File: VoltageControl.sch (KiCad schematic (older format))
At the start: 7 parts, among them U201 LMV358

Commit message: updated schematic capacitor symbols to use new default library symbols
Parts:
- C201: Fieldname (none) -> Value
- R201, R202, R203: symbol R -> R-RESCUE-CurrentSinkOrSwim
- RV201: symbol POT -> POT-RESCUE-CurrentSinkOrSwim
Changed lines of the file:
@@
 EESchema Schematic File Version 2
+LIBS:CurrentSinkOrSwim-rescue
 LIBS:power
 LIBS:device
@@
 LIBS:memory
 LIBS:xilinx
-LIBS:special
 LIBS:microcontrollers
 LIBS:dsp
@@
 $EndComp
 $Comp
-L R R201
+L R-RESCUE-CurrentSinkOrSwim R201
 U 1 1 54DB1D0A
 P 4100 2650
@@
 	3800 5550 9850 5550
 $Comp
-L POT RV201
+L POT-RESCUE-CurrentSinkOrSwim RV201
 U 1 1 54DB1D22
 P 3800 3550
@@
 	1    0    0    -1
 $EndComp
-$Comp
-L C C201
-U 1 1 54DB1D32
-P 5150 2400
-F 0 "C201" H 5200 2500 50  0000 L CNN
-F 1 ".1" H 5200 2300 50  0000 L CNN
-F 2 "SMD_Packages:SMD-0805" H 5188 2250 30  0001 C CNN
-F 3 "" H 5150 2400 60  0000 C CNN
-	1    5150 2400
-	1    0    0    -1
-$EndComp
 Wire Wire Line
 	5150 1950 5150 2200
 Connection ~ 5150 1950
-Wire Wire Line
-	5150 2650 5150 2600
 Text GLabel 2650 1350 0    60   Input ~ 0
 2.7V
@@
 $EndComp
 $Comp
-L R R202
+L R-RESCUE-CurrentSinkOrSwim R202
 U 1 1 54DB1EC2
 P 8700 3450
@@
 $EndComp
 $Comp
-L R R203
+L R-RESCUE-CurrentSinkOrSwim R203
 U 1 1 54DB1F3A
 P 8700 4300
@@
 	4100 2900 4100 3550
 Connection ~ 4100 3550
+$Comp
+L C C201
+U 1 1 57B0D6FD
+P 5150 2350
+F 0 "C201" H 5175 2450 50  0000 L CNN
+F 1 ".1" H 5175 2250 50  0000 L CNN
+F 2 "SMD_Packages:SMD-0805" H 5188 2200 50  0001 C CNN
+F 3 "" H 5150 2350 50  0000 C CNN
+F 4 "Value" H 5150 2350 60  0001 C CNN "Fieldname"
+	1    5150 2350
+	1    0    0    -1
+$EndComp
+Wire Wire Line
+	5150 2500 5150 2650
 $EndSCHEMATC

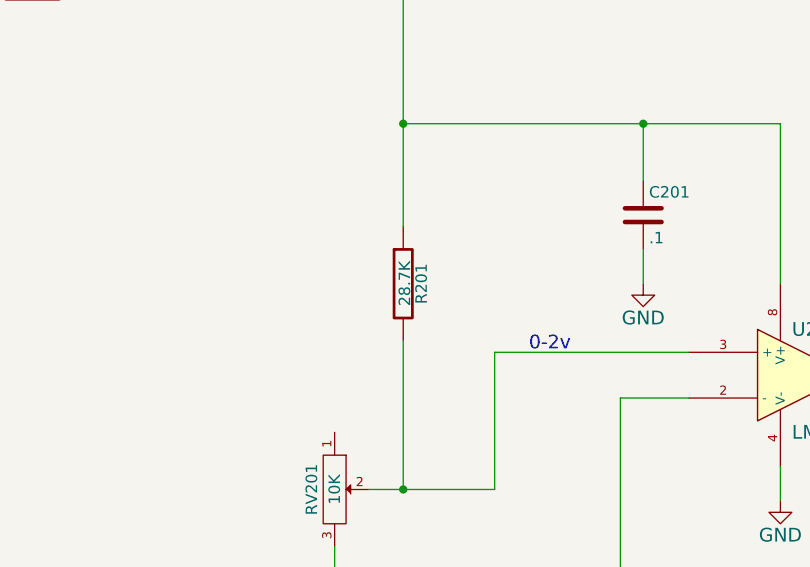
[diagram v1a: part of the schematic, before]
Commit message: corrected cap on voltage regulator and corrected voltage divider in voltage control
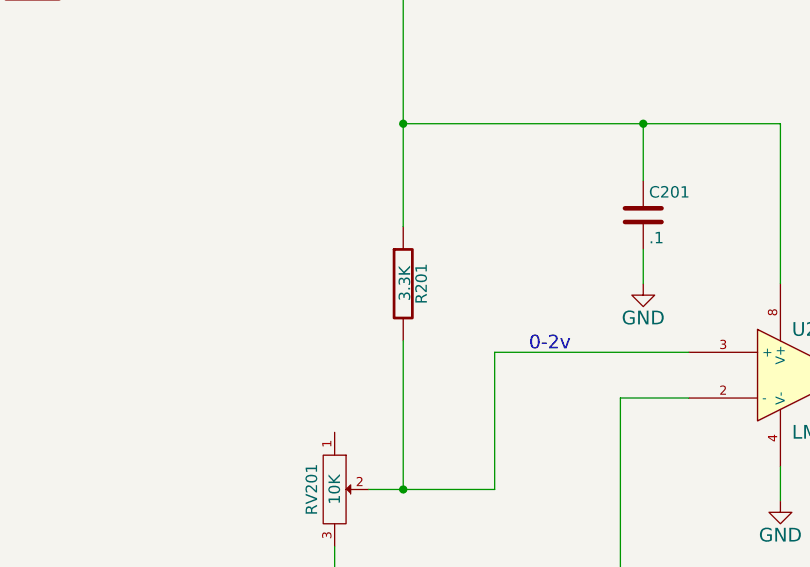
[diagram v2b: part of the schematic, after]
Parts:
- R201: value 28.7K -> 3.3K
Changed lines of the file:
@@
 EESchema Schematic File Version 2
-LIBS:CurrentSinkOrSwim-rescue
 LIBS:power
 LIBS:device
@@
 P 4100 2650
 F 0 "R201" V 4180 2650 50  0000 C CNN
-F 1 "28.7K" V 4107 2651 50  0000 C CNN
+F 1 "3.3K" V 4107 2651 50  0000 C CNN
 F 2 "SMD_Packages:SMD-0805" V 4030 2650 30  0001 C CNN
 F 3 "" H 4100 2650 30  0000 C CNN

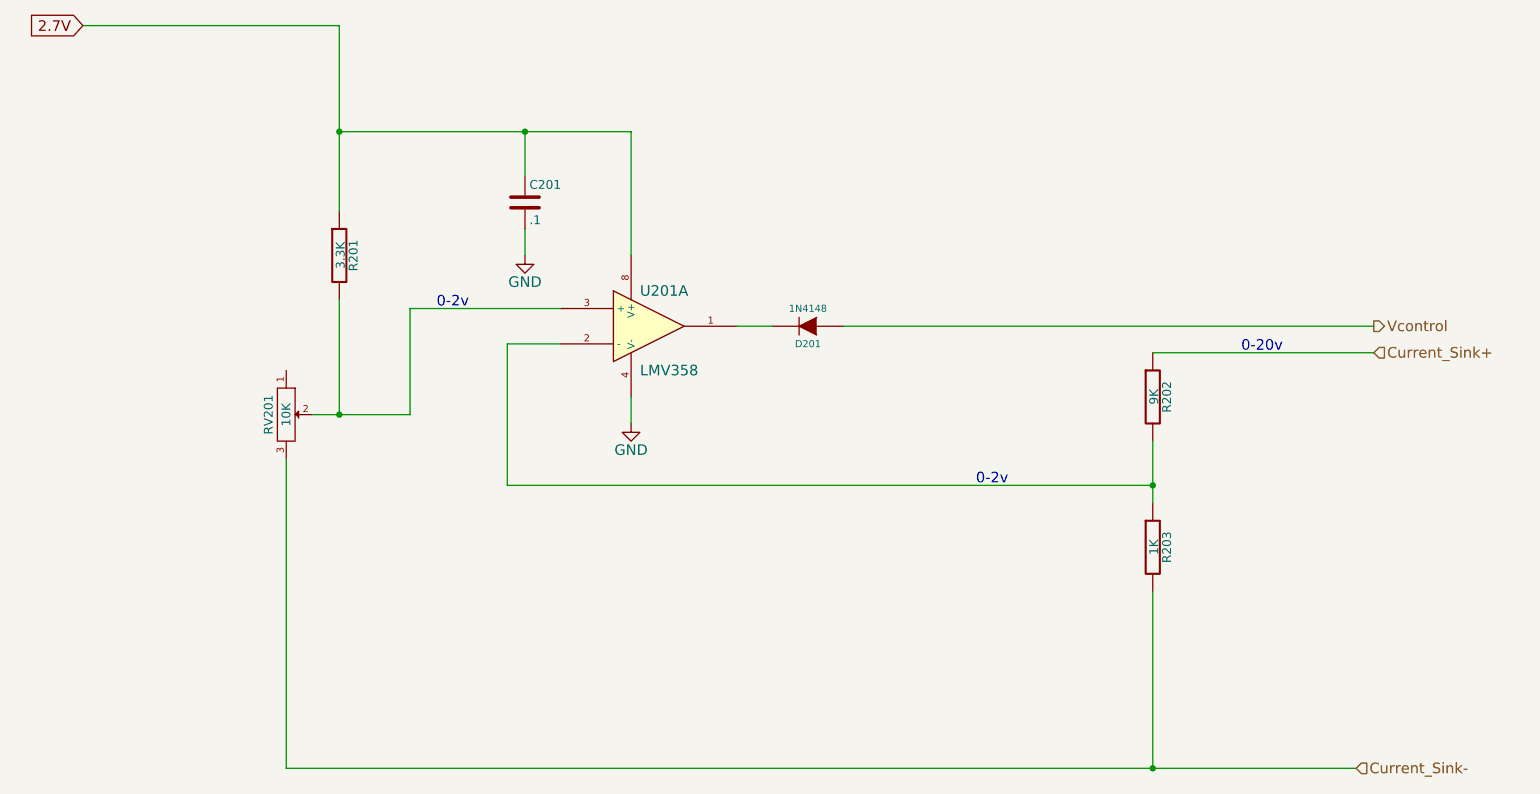
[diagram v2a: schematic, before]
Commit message: updated diode to sod-323 package and used new schematic symbol because pin numbers changed
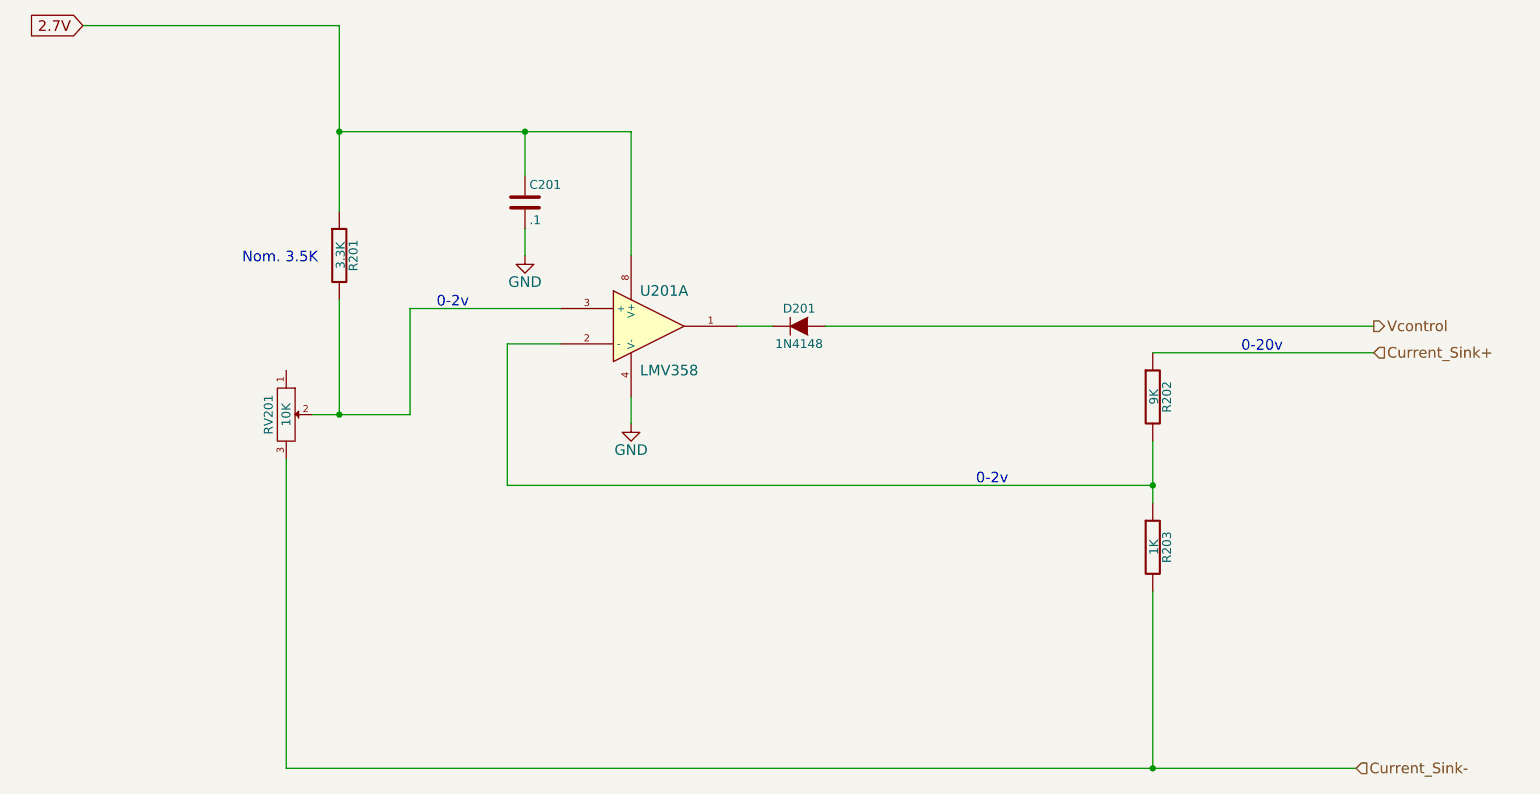
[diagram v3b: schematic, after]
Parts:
- removed D201: 1N4148, SMD_Packages:SOD-523, symbol DIODE
- added D201: 1N4148, Diodes_SMD:SOD-323, symbol D
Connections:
- net Vcontrol: now also D201.2 (A)
- net at U201.1: now also D201.1 (K)
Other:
- note added: "Nom. 3.5K"
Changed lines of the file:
@@
 	6350 3050 6550 3050
-$Comp
-L DIODE D201
-U 1 1 54DB1E38
-P 6750 3050
-F 0 "D201" H 6750 3150 40  0000 C CNN
-F 1 "1N4148" H 6750 2950 40  0000 C CNN
-F 2 "SMD_Packages:SOD-523" H 6750 3050 60  0001 C CNN
-F 3 "http://www.diodes.com/datasheets/ds30396.pdf" H 6750 3050 60  0001 C CNN
-F 4 "1N4148WT-7" H 6750 3050 60  0001 C CNN "MPN"
-	1    6750 3050
-	-1   0    0    1
-$EndComp
 $Comp
 L R-RESCUE-CurrentSinkOrSwim R202
@@
 Connection ~ 8700 3950
 Wire Wire Line
-	6950 3050 9950 3050
+	6850 3050 9950 3050
 Text HLabel 9950 3050 2    60   Output ~ 0
 Vcontrol
@@
 Wire Wire Line
 	5150 2500 5150 2650
+Text Notes 3550 2700 0    60   ~ 0
+Nom. 3.5K
+$Comp
+L D D201
+U 1 1 57BA579F
+P 6700 3050
+F 0 "D201" H 6700 3150 50  0000 C CNN
+F 1 "1N4148" H 6700 2950 50  0000 C CNN
+F 2 "Diodes_SMD:SOD-323" H 6700 3050 50  0001 C CNN
+F 3 "http://www.diodes.com/_files/datasheets/ds30097.pdf" H 6700 3050 50  0001 C CNN
+F 4 "Value" H 6700 3050 60  0001 C CNN "Fieldname"
+F 5 "1N4148WS-7-F" H 6700 3050 60  0001 C CNN "MPN"
+	1    6700 3050
+	1    0    0    -1
+$EndComp
 $EndSCHEMATC

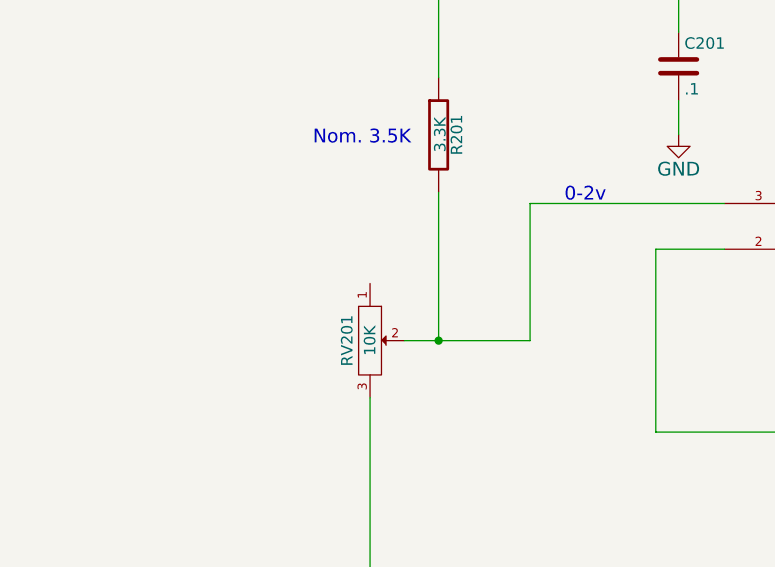
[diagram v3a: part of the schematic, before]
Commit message: added 100uF pcb footprint and misc comments
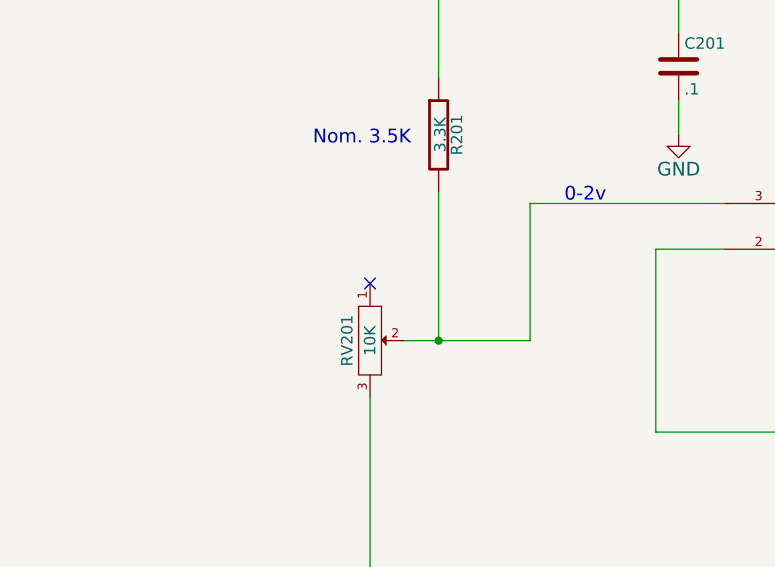
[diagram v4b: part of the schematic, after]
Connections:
- no-connect marks 0 -> 1
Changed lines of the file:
@@
 	1    0    0    -1
 $EndComp
+NoConn ~ 3800 3300
 $EndSCHEMATC

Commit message: initial component placement on the pcb
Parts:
- C201: footprint SMD_Packages:SMD-0805 -> Capacitors_SMD:C_0805
- R201, R202, R203: footprint SMD_Packages:SMD-0805 -> Resistors_SMD:R_0805
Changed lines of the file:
@@
 F 0 "R201" V 4180 2650 50  0000 C CNN
 F 1 "3.3K" V 4107 2651 50  0000 C CNN
-F 2 "SMD_Packages:SMD-0805" V 4030 2650 30  0001 C CNN
+F 2 "Resistors_SMD:R_0805" V 4030 2650 30  0001 C CNN
 F 3 "" H 4100 2650 30  0000 C CNN
 	1    4100 2650
@@
 F 0 "R202" V 8780 3450 50  0000 C CNN
 F 1 "9K" V 8707 3451 50  0000 C CNN
-F 2 "SMD_Packages:SMD-0805" V 8630 3450 30  0001 C CNN
+F 2 "Resistors_SMD:R_0805" V 8630 3450 30  0001 C CNN
 F 3 "" H 8700 3450 30  0000 C CNN
 	1    8700 3450
@@
 F 0 "R203" V 8780 4300 50  0000 C CNN
 F 1 "1K" V 8707 4301 50  0000 C CNN
-F 2 "SMD_Packages:SMD-0805" V 8630 4300 30  0001 C CNN
+F 2 "Resistors_SMD:R_0805" V 8630 4300 30  0001 C CNN
 F 3 "" H 8700 4300 30  0000 C CNN
 	1    8700 4300
@@
 F 0 "C201" H 5175 2450 50  0000 L CNN
 F 1 ".1" H 5175 2250 50  0000 L CNN
-F 2 "SMD_Packages:SMD-0805" H 5188 2200 50  0001 C CNN
+F 2 "Capacitors_SMD:C_0805" H 5188 2200 50  0001 C CNN
 F 3 "" H 5150 2350 50  0000 C CNN
 F 4 "Value" H 5150 2350 60  0001 C CNN "Fieldname"

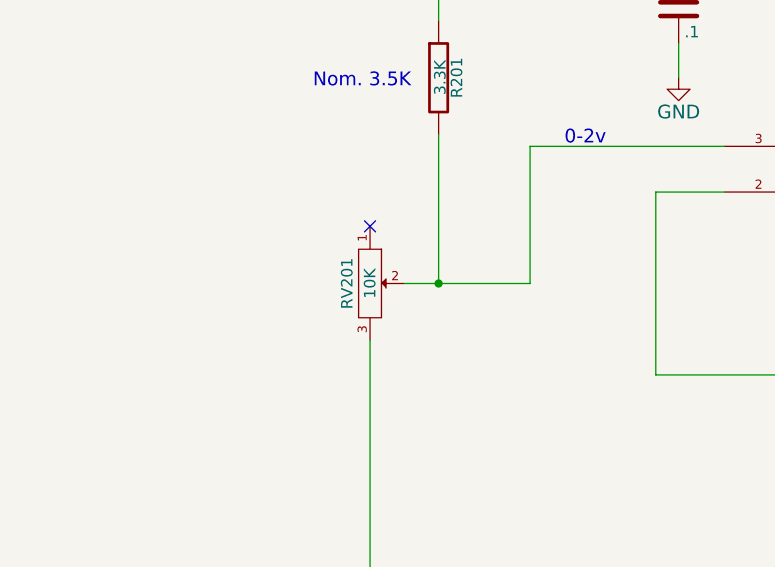
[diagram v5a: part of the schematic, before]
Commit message: added labels, switched leads on voltage pot so + == clockwise, enlarged ground plane
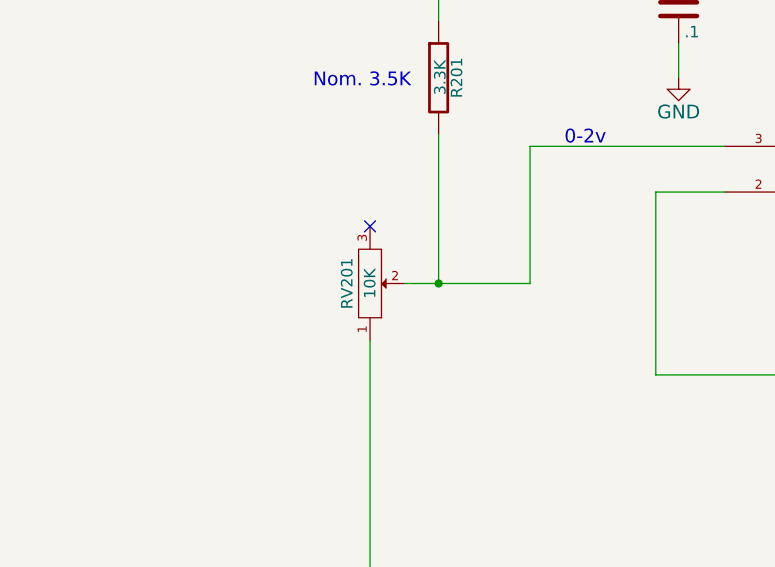
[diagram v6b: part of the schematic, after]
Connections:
- net Current_Sink-: now also RV201.1; no longer RV201.3
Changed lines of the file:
@@
 F 4 "P090L-02F25BR10K" H 3800 3550 60  0001 C CNN "MPN"
 	1    3800 3550
-	0    1    1    0
+	0    1    -1   0
 $EndComp
 Wire Wire Line

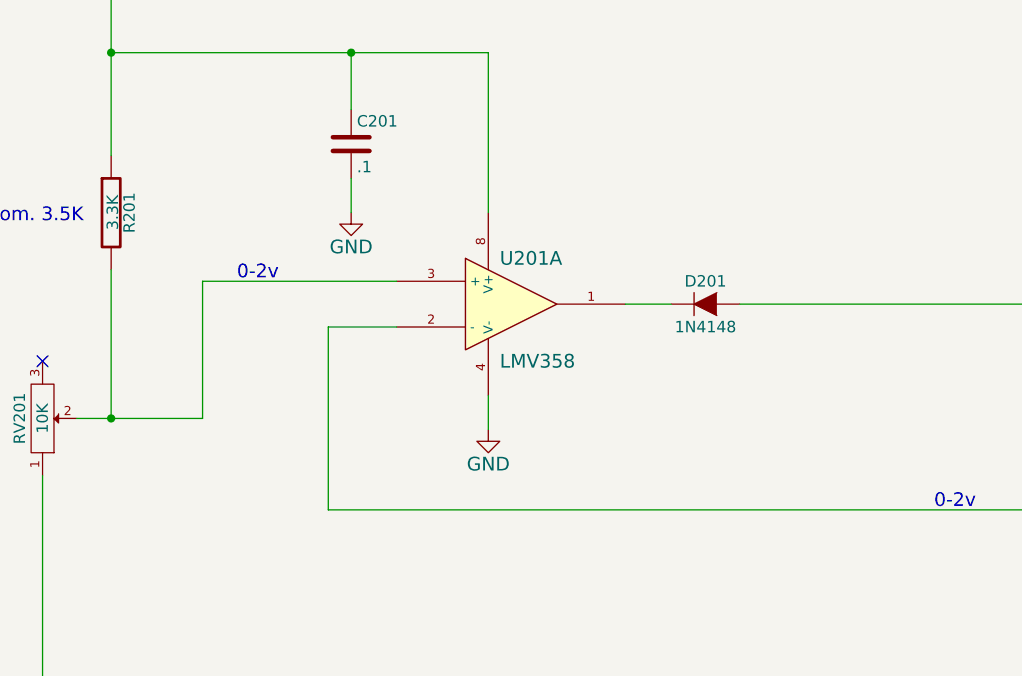
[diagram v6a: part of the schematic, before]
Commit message: added test points to  schematic and pcb
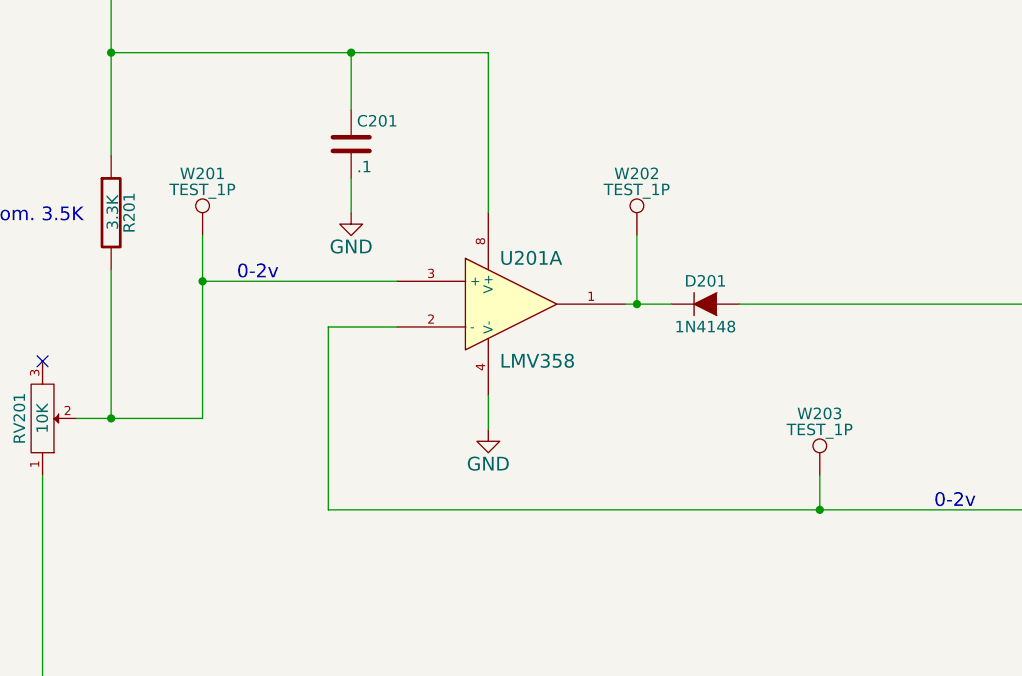
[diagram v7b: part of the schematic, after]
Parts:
- added W201, W202, W203: TEST_1P, Measurement_Points:Measurement_Point_Round-SMD-Pad_Small, symbol TEST_1P
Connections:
- net at D201.1 (K), U201.1: now also W202.1
- net at R202.2, R203.1, U201.2 (-): now also W203.1
- net at R201.2, RV201.2, U201.3 (+): now also W201.1
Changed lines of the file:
@@
 	4100 1950 5750 1950
 Wire Wire Line
-	4500 2950 4500 3550
+	4500 2750 4500 3550
 Text Notes 4650 2950 0    60   ~ 0
 0-2v
@@
 $EndComp
 NoConn ~ 3800 3300
+$Comp
+L TEST_1P W202
+U 1 1 57C8594F
+P 6400 2750
+F 0 "W202" H 6400 3020 50  0000 C CNN
+F 1 "TEST_1P" H 6400 2950 50  0000 C CNN
+F 2 "Measurement_Points:Measurement_Point_Round-SMD-Pad_Small" H 6600 2750 50  0001 C CNN
+F 3 "" H 6600 2750 50  0000 C CNN
+	1    6400 2750
+	1    0    0    -1
+$EndComp
+Wire Wire Line
+	6400 2750 6400 3050
+Connection ~ 6400 3050
+$Comp
+L TEST_1P W201
+U 1 1 57C859C5
+P 4500 2750
+F 0 "W201" H 4500 3020 50  0000 C CNN
+F 1 "TEST_1P" H 4500 2950 50  0000 C CNN
+F 2 "Measurement_Points:Measurement_Point_Round-SMD-Pad_Small" H 4700 2750 50  0001 C CNN
+F 3 "" H 4700 2750 50  0000 C CNN
+	1    4500 2750
+	1    0    0    -1
+$EndComp
+Connection ~ 4500 2950
+$Comp
+L TEST_1P W203
+U 1 1 57C85A59
+P 7200 3800
+F 0 "W203" H 7200 4070 50  0000 C CNN
+F 1 "TEST_1P" H 7200 4000 50  0000 C CNN
+F 2 "Measurement_Points:Measurement_Point_Round-SMD-Pad_Small" H 7400 3800 50  0001 C CNN
+F 3 "" H 7400 3800 50  0000 C CNN
+	1    7200 3800
+	1    0    0    -1
+$EndComp
+Wire Wire Line
+	7200 3800 7200 3950
+Connection ~ 7200 3950
 $EndSCHEMATC
